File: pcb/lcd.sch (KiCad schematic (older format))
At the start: 1 part, among them J1 ITDB_TFT

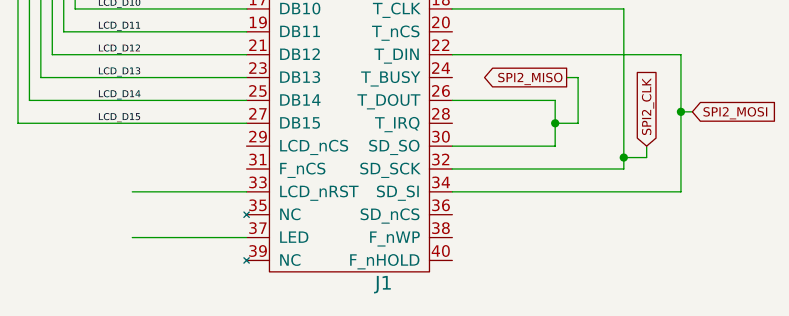
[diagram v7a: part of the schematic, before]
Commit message: Reannoted everything so that there isn't any duplicates. Also added connection to the rf reset line.
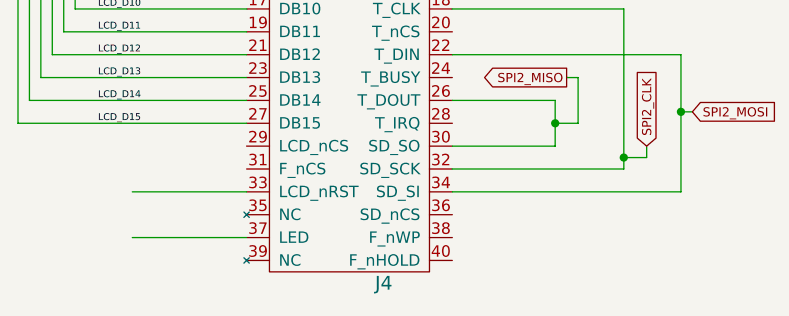
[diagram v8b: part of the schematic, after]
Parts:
- renumbered J1 to J4
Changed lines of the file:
@@
-EESchema Schematic File Version 2  date 10/10/2012 1:41:54 PM
+EESchema Schematic File Version 2  date 10/11/2012 11:52:24 AM
 LIBS:power
 LIBS:device
@@
 Sheet 5 7
 Title ""
-Date "10 oct 2012"
+Date "11 oct 2012"
 Rev ""
 Comp ""
@@
 	4950 2900 5050 3000
 $Comp
-L GND #PWR28
+L GND #PWR30
 U 1 1 50188B84
 P 3850 3500
-F 0 "#PWR28" H 3850 3500 30  0001 C CNN
+F 0 "#PWR30" H 3850 3500 30  0001 C CNN
 F 1 "GND" H 3850 3430 30  0001 C CNN
 	1    3850 3500
@@
 Vreg
 $Comp
-L ITDB_TFT J1
+L ITDB_TFT J4
 U 1 1 50188B83
 P 4850 4300
-F 0 "J1" H 5000 3200 60  0000 C CNN
+F 0 "J4" H 5000 3200 60  0000 C CNN
 F 1 "ITDB_TFT" H 4850 5300 60  0000 C CNN
 	1    4850 4300
